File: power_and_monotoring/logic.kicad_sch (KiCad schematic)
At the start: 55 parts, among them Q1 DMN6075SQ-7, U2 LM7902D, U3 LM7902D, U4 LM7902D, U6 CD4081BM96, U7 CD4071BM96

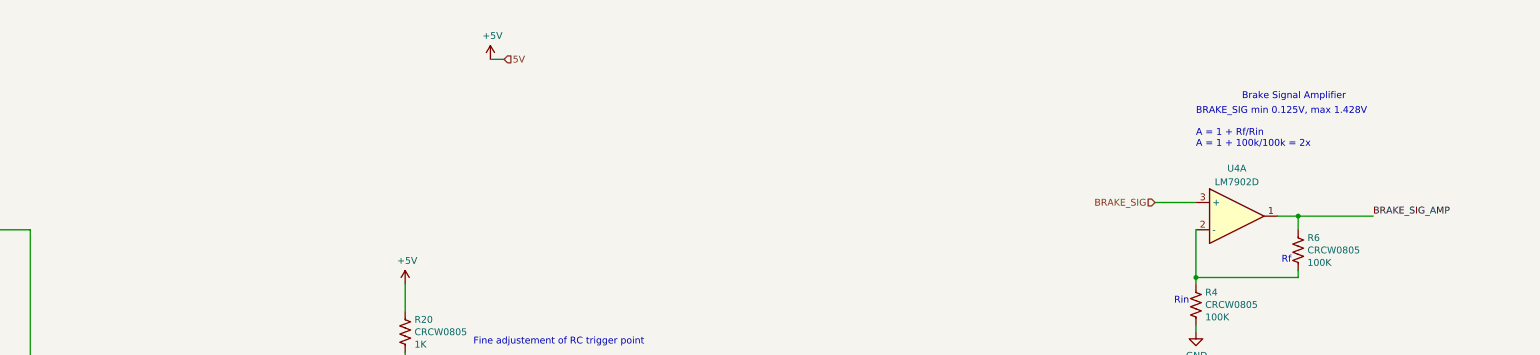
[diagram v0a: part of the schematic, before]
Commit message: first connections done (not perfect yet)
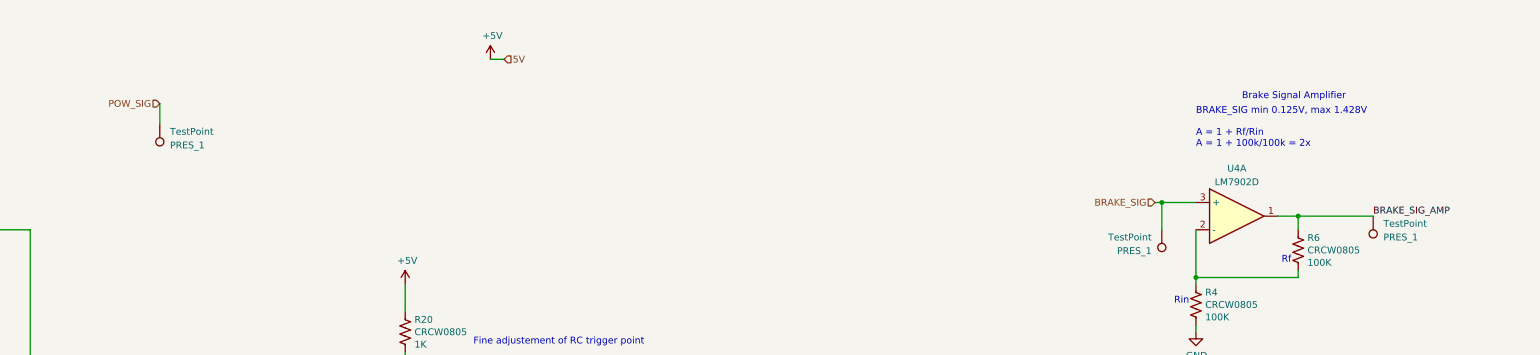
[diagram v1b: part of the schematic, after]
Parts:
- added PRES_1 (x3): TestPoint, TestPoint:TestPoint_Pad_D2.0mm, symbol Connector:TestPoint
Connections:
- net BRAKE_SIG: now also PRES_1.1
- net BRAKE_SIG_AMP: now also PRES_1.1
- net POW_SIG: now also PRES_1.1
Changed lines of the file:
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@@
   (junction (at 55.245 90.17) (diameter 0) (color 0 0 0 0)
   )
+  (junction (at 373.38 67.31) (diameter 0) (color 0 0 0 0)
+  )
   (junction (at 238.76 227.965) (diameter 0) (color 0 0 0 0)
   )
@@
     (stroke (width 0) (type default))
   )
+  (wire (pts (xy 373.38 67.31) (xy 373.38 72.39))
+    (stroke (width 0) (type default))
+  )
   (wire (pts (xy 105.41 248.92) (xy 105.41 247.65))
     (stroke (width 0) (type default))
@@
     (stroke (width 0) (type default))
   )
+  (wire (pts (xy 373.38 67.31) (xy 372.11 67.31))
+    (stroke (width 0) (type default))
+  )
   (wire (pts (xy 398.78 69.85) (xy 412.75 69.85))
     (stroke (width 0) (type default))
@@
     (stroke (width 0) (type default))
   )
+  (wire (pts (xy 186.69 48.895) (xy 186.69 52.705))
+    (stroke (width 0) (type default))
+  )
   (wire (pts (xy 105.41 161.29) (xy 105.41 161.417))
     (stroke (width 0) (type default))
@@
     (stroke (width 0) (type default))
   )
-  (wire (pts (xy 379.73 67.31) (xy 372.11 67.31))
+  (wire (pts (xy 379.73 67.31) (xy 373.38 67.31))
     (stroke (width 0) (type default))
   )
@@
     (effects (font (size 1.27 1.27)) (justify left))
   )
+  (hierarchical_label "POW_SIG" (shape input) (at 186.69 48.895 180) (fields_autoplaced)
+    (effects (font (size 1.27 1.27)) (justify right))
+  )
   (hierarchical_label "POW_SIG" (shape input) (at 67.31 53.34 180) (fields_autoplaced)
     (effects (font (size 1.27 1.27)) (justify right))
@@
     )
   )
+  (symbol (lib_id "Connector:TestPoint") (at 186.69 52.705 180) (unit 1)
+    (in_bom yes) (on_board yes) (dnp no)
+    (property "Reference" "PRES_1" (at 188.595 56.642 0)
+      (effects (font (size 1.27 1.27)) (justify right))
+    )
+    (property "Value" "TestPoint" (at 188.595 54.102 0)
+      (effects (font (size 1.27 1.27)) (justify right))
+    )
+    (property "Footprint" "TestPoint:TestPoint_Pad_D2.0mm" (at 181.61 52.705 0)
+      (effects (font (size 1.27 1.27)) hide)
+    )
+    (property "Datasheet" "~" (at 181.61 52.705 0)
+      (effects (font (size 1.27 1.27)) hide)
+    )
+    (pin "1")
+    (instances
+      (project "power_and_monotoring"
+        (path "/09bdaed7-9abd-4a06-aca9-25dcfc39eec3/52a30286-526e-4683-a1ba-aa6f0bb5d9ff"
+          (reference "PRES_1") (unit 1)
+        )
+        (path "/09bdaed7-9abd-4a06-aca9-25dcfc39eec3/22f29577-e4ea-44ad-b176-4b72d277bfff"
+          (reference "POW_SIG1") (unit 1)
+        )
+      )
+      (project "FeatherBoard"
+        (path "/e63e39d7-6ac0-4ffd-8aa3-1841a4541b55/ce4178aa-a44b-4063-8e1c-03c90baefe49"
+          (reference "TP1") (unit 1)
+        )
+      )
+    )
+  )
   (symbol (lib_id "power:GND") (at 259.08 277.495 0) (unit 1)
     (in_bom yes) (on_board yes) (dnp no)
@@
     )
   )
+  (symbol (lib_id "Connector:TestPoint") (at 373.38 72.39 0) (mirror x) (unit 1)
+    (in_bom yes) (on_board yes) (dnp no)
+    (property "Reference" "PRES_1" (at 371.475 76.327 0)
+      (effects (font (size 1.27 1.27)) (justify right))
+    )
+    (property "Value" "TestPoint" (at 371.475 73.787 0)
+      (effects (font (size 1.27 1.27)) (justify right))
+    )
+    (property "Footprint" "TestPoint:TestPoint_Pad_D2.0mm" (at 378.46 72.39 0)
+      (effects (font (size 1.27 1.27)) hide)
+    )
+    (property "Datasheet" "~" (at 378.46 72.39 0)
+      (effects (font (size 1.27 1.27)) hide)
+    )
+    (pin "1")
+    (instances
+      (project "power_and_monotoring"
+        (path "/09bdaed7-9abd-4a06-aca9-25dcfc39eec3/52a30286-526e-4683-a1ba-aa6f0bb5d9ff"
+          (reference "PRES_1") (unit 1)
+        )
+        (path "/09bdaed7-9abd-4a06-aca9-25dcfc39eec3/22f29577-e4ea-44ad-b176-4b72d277bfff"
+          (reference "BRAKE_SIG1") (unit 1)
+        )
+      )
+      (project "FeatherBoard"
+        (path "/e63e39d7-6ac0-4ffd-8aa3-1841a4541b55/ce4178aa-a44b-4063-8e1c-03c90baefe49"
+          (reference "TP1") (unit 1)
+        )
+      )
+    )
+  )
   (symbol (lib_name "+5V_1") (lib_id "power:+5V") (at 248.285 40.64 0) (unit 1)
     (in_bom yes) (on_board yes) (dnp no)
@@
         )
       )
+    )
+  )
+  (symbol (lib_id "Connector:TestPoint") (at 412.75 69.85 180) (unit 1)
+    (in_bom yes) (on_board yes) (dnp no)
+    (property "Reference" "PRES_1" (at 414.655 73.787 0)
+      (effects (font (size 1.27 1.27)) (justify right))
+    )
+    (property "Value" "TestPoint" (at 414.655 71.247 0)
+      (effects (font (size 1.27 1.27)) (justify right))
+    )
+    (property "Footprint" "TestPoint:TestPoint_Pad_D2.0mm" (at 407.67 69.85 0)
+      (effects (font (size 1.27 1.27)) hide)
+    )
+    (property "Datasheet" "~" (at 407.67 69.85 0)
+      (effects (font (size 1.27 1.27)) hide)
+    )
+    (pin "1")
+    (instances
+      (project "power_and_monotoring"
+        (path "/09bdaed7-9abd-4a06-aca9-25dcfc39eec3/52a30286-526e-4683-a1ba-aa6f0bb5d9ff"
+          (reference "PRES_1") (unit 1)
+        )
+        (path "/09bdaed7-9abd-4a06-aca9-25dcfc39eec3/22f29577-e4ea-44ad-b176-4b72d277bfff"
+          (reference "BRAKE_SIG_AMP1") (unit 1)
+        )
+      )
+      (project "FeatherBoard"
+        (path "/e63e39d7-6ac0-4ffd-8aa3-1841a4541b55/ce4178aa-a44b-4063-8e1c-03c90baefe49"
+          (reference "TP1") (unit 1)
+        )
+      )

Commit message: before design review
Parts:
- removed LED1, LED2, LED3, LED4, LED5, LED6, LED7: RED, LTST-S270KRKT, UniSA_Motorsport_Diode:0605, symbol UniSA_Motorsport_Diode:LTST-S270KRKT
- removed LED8: GREEN, LTST-S270KGKT, UniSA_Motorsport_Diode:0605, symbol UniSA_Motorsport_Diode:LTST-S270KGKT
- removed RV15 (x8): 10K, UniSA_Motorsport_Others:3296X_POT, symbol UniSA_Motorsport_Resistor:3296X-1-103LF
- added D1, D2, D3, D4, D5, D6, D7: RED, UniSA_Motorsport_Diode:0805, symbol UniSA_Motorsport_Diode:LED_0805
- added D8: GREEN, UniSA_Motorsport_Diode:0805, symbol UniSA_Motorsport_Diode:LED_0805
- added J6: 43045-1015, UniSA_Motorsport_Connector:MOLEX_43045-10YY_10PIN, symbol UniSA_Motorsport_Connector:43045-1015
- added RL1, RL2, RL3, RL4, RL5, RL6, RL7, RL8: 10 K, UniSA_Motorsport_Resistor:3296W-1, symbol UniSA_Motorsport_Resistor:3296W-1-103LF
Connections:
- net +5V: now also RL3.1, RL5.1
- net BRAKE_LIGHT_SIG: now also D8.2 (A), J6.8 (Pin_8)
- net BRAKE_SIG_AMP_HIGH: now also D2.2 (A), J6.2 (Pin_2)
- net BRAKE_SIG_AMP_SHORT_GND: now also D6.2 (A), J6.6 (Pin_6)
- net BRAKE_SIG_AMP_SHORT_HIGH: now also D5.2 (A), J6.5 (Pin_5)
- net D_BSPD_TRIGGER: now also D7.2 (A), J6.7 (Pin_7)
- net GND: now also D1.1 (K), D2.1 (K), D3.1 (K), D4.1 (K), D5.1 (K), D6.1 (K), D7.1 (K), D8.1 (K), J6.10 (Pin_10), J6.9 (Pin_9), RL1.3, RL2.3, RL4.3, RL6.3, RL7.3, RL8.3
- net POWER_SIG_HIGH: now also D1.2 (A), J6.1 (Pin_1)
- net POWER_SIG_SHORT_GND: now also D4.2 (A), J6.4 (Pin_4)
- net POWER_SIG_SHORT_HIGH: now also D3.2 (A), J6.3 (Pin_3)
- net at R20.2: now also RL7.1
- net at PRES_1.1, U3.12 (+): now also RL7.2
- net at R3.2: now also RL8.1
- net at PRES_1.1, U2.6 (-): now also RL1.2
- net at PRES_1.1, U2.13 (-): now also RL3.2
- net at R9.1: now also RL3.3
- net at PRES_1.1, U3.6 (-): now also RL5.2
- net at PRES_1.1, U3.3 (+): now also RL4.2
- net at R11.1: now also RL5.3
- net at R10.2: now also RL4.1
- net at R8.2: now also RL2.1
- net at PRES_1.1, U2.2 (-): now also RL8.2
- net at R12.2: now also RL6.1
- net at PRES_1.1, U3.10 (+): now also RL6.2
- net at PRES_1.1, U2.9 (-): now also RL2.2
- net at R7.2: now also RL1.1

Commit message: Final
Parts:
- removed C3: GCM0805_1u, UniSA_Motorsport_Capacitor:0805, symbol UniSA_Motorsport_Capacitor:GCM0805_1u
- removed PRES_1: TestPoint, TestPoint:TestPoint_Pad_D2.0mm, symbol Connector:TestPoint
- removed R10, R11, R12, R20, R8, R9: CRCW0805, UniSA_Motorsport_Resistor:0805, symbol UniSA_Motorsport_Resistor:CRCW0805
- removed U6: CD4081BM96, UniSA_Motorsport_SO:SOIC-14, symbol UniSA_Motorsport_Logic:CD4081BM96
- added BRAKE_SIG_AMP1: TestPoint, TestPoint:TestPoint_Pad_D2.0mm, symbol Connector:TestPoint
- added R29, R30, R50, R51: CRCW0805, UniSA_Motorsport_Resistor:0805, symbol UniSA_Motorsport_Resistor:CRCW0805
- added U1: 74LVC1G08GW,125, UniSA_Motorsport_SO:TSSOP-5, symbol UniSA_Motorsport_Logic:74LVC1G08GW,125
- R13, R14, R15, R16, R17, R18: Resistance 150R -> 470R
- R21, R5: Resistance 100R -> 470R
- R3: Resistance 1K -> 2.2K
- R4, R6: Resistance 100K -> 10K
- renumbered PRES_1 to BRAKE_SIG1, PRES_1 to BREAK_HIGH1, PRES_1 to BREAK_LOW1, PRES_1 to BREAK_PRESSED1, PRES_1 to BREAK_SIG1, C4 to C2, C4 to C3, C4 to C5, D7 to D1, D1 to D2, D2 to D3, D3 to D4, D4 to D5, D5 to D6, D6 to D7, PRES_1 to POW_HIGH1, PRES_1 to POW_LOW1, PRES_1 to POW_PRESSED1, PRES_1 to POW_SIG_AMP1, PRES_1 to RC_TRIG1
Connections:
- net +5V: now also U1.5 (VCC); no longer C5.1, R3.1, R7.1, RL3.1, RL5.1, U4.4 (VDD)
- net BRAKE_LIGHT_SIG: now also Q1.1 (G), R5.1, U2.1; no longer D8.2 (A), R5.2
- net BRAKE_SIG_AMP: now also U4.13 (-), U4.14, BRAKE_SIG_AMP1.1; no longer R6.1, U4.1
- net BRAKE_SIG_AMP_HIGH: now also R14.1, U2.8, U1.2; no longer D3.2 (A), R14.2
- net BRAKE_SIG_AMP_SHORT_GND: now also R18.1, U3.8, U7.6; no longer D7.2 (A), R18.2
- net BRAKE_SIG_AMP_SHORT_HIGH: now also R17.1, U3.7, U7.5; no longer D6.2 (A), R17.2
- net BSPD_TRIGGER: now also J6.7 (Pin_7)
- net GND: now also R3.2, RL3.3, RL5.3, R30.2, R51.2, U1.3 (GND); no longer U4.10 (+), U4.12 (+), U4.5 (+)
- net POWER_SIG_HIGH: now also R13.1, U2.7, U1.1; no longer D2.2 (A), R13.2
- net POWER_SIG_SHORT_GND: now also R16.1, U3.1, U7.2; no longer D5.2 (A), R16.2
- net POWER_SIG_SHORT_HIGH: now also R15.1, U2.14, U7.1; no longer D4.2 (A), R15.2
- net POW_SIG: now also U4.5 (+); no longer POW_SIG_AMP1.1, U2.12 (+), U2.5 (+), U3.2 (-)
- net +3.3V: now reaches RL8.1
- net +3.3V: now also RL1.1, RL2.1, RL3.1, RL4.1, RL5.1, RL6.1, RL7.1; no longer R3.2
- net at U7.12: now also U1.4
- net at R7.2: now also R19.1, R3.1; no longer RL1.1
- net POW_SIG_AMP: now reaches U4.8, U4.9 (-)
- net POW_SIG_AMP: now also POW_SIG_AMP1.1, U2.12 (+), U2.5 (+), U3.2 (-)
- net at U7.11: now also R7.1; no longer R19.1
- net at U4.6 (-), U4.7: now also R29.1
- net D_BSPD_TRIGGER: no longer names the net of D1.2 (A), R21.2
- net D_BSPD_TRIGGER: no longer J6.7 (Pin_7)
- new net: D4.2 (A), R15.2
- new net: D7.2 (A), R18.2
- new net: D8.2 (A), R5.2
- new net: R29.2, R30.1, U4.10 (+)
- new net: D2.2 (A), R13.2
- new net: R50.1, R6.1, U4.1
- new net: R50.2, R51.1, U4.12 (+)
- new net: D5.2 (A), R16.2
- new net: D6.2 (A), R17.2
- new net: D3.2 (A), R14.2
- new net 12V: C5.1, U4.4 (VDD)
- no-connect marks 3 -> 0
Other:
- note added: "Leave unconected"
- note added: "R1"
- note added: "R2"
- note added: "Vout=Vin*(R2)/(R1+R2)"
- note removed: "Unused Logic"
- moved on the sheet: BRAKE_SIG1, J6, POW_SIG_AMP1, R4, R6, U4A, U4B, U4C, U4D

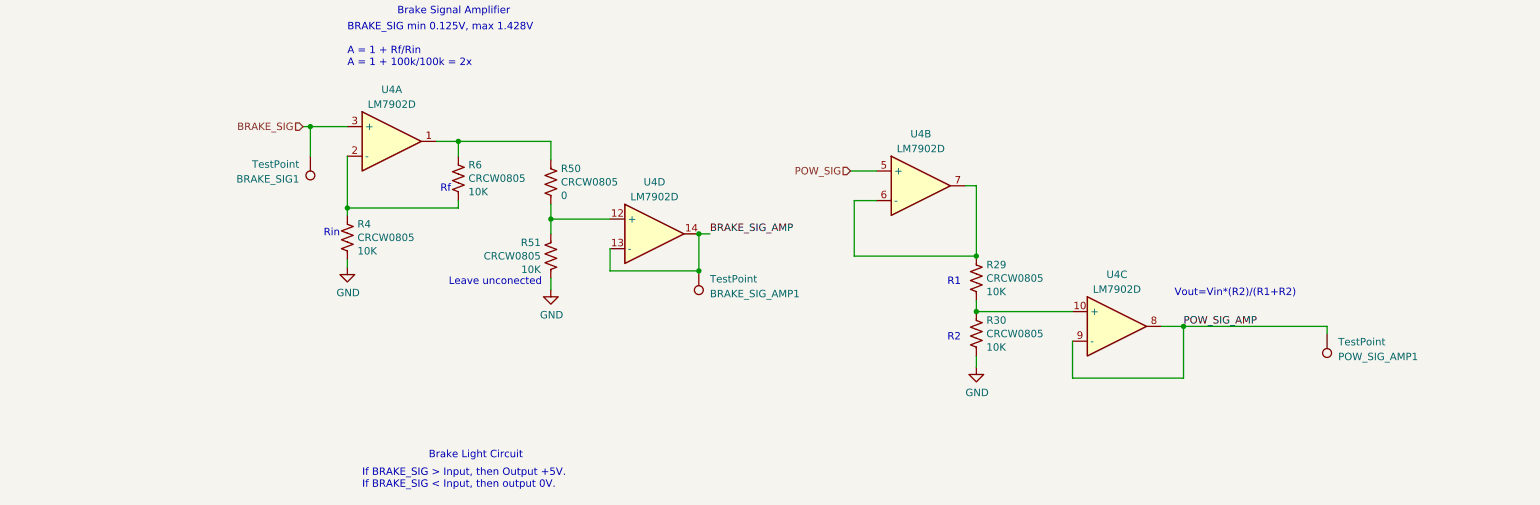
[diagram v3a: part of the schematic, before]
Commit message: Made it 4 layers
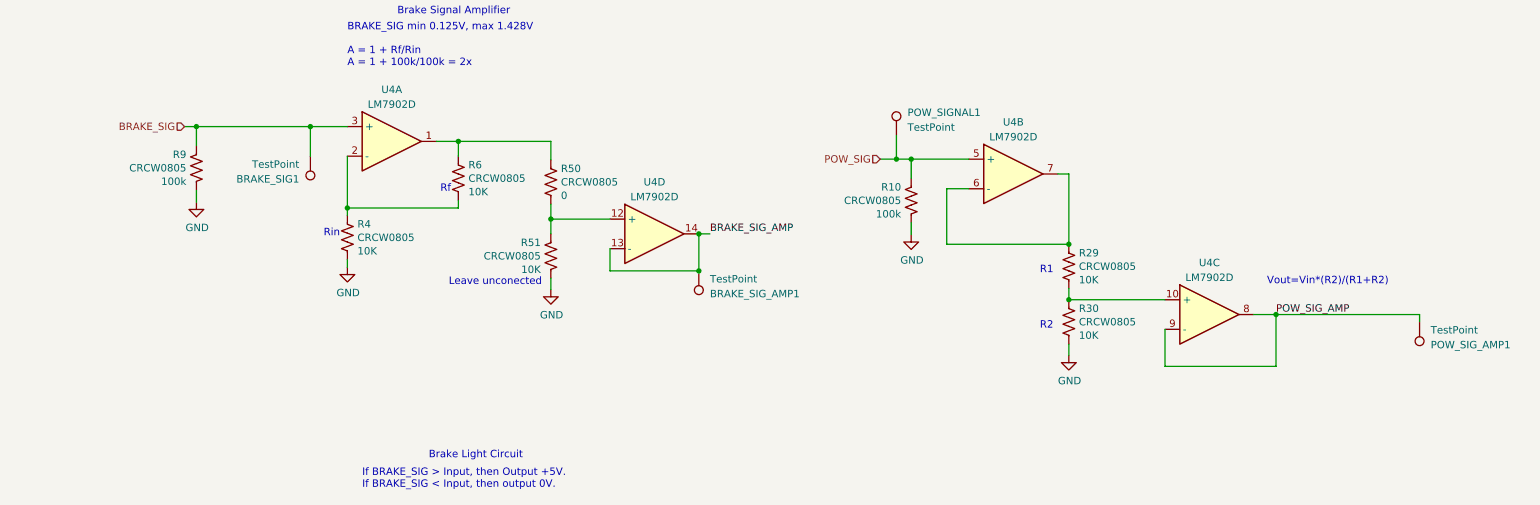
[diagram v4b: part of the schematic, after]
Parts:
- added POW_SIGNAL1: TestPoint, TestPoint:TestPoint_Pad_D2.0mm, symbol Connector:TestPoint
- added R10, R9: CRCW0805, UniSA_Motorsport_Resistor:0805, symbol UniSA_Motorsport_Resistor:CRCW0805
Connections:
- net BRAKE_SIG: now also R9.1
- net GND: now also R10.2, R9.2
- net POW_SIG: now also POW_SIGNAL1.1, R10.1
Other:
- moved on the sheet: POW_SIG_AMP1, R29, R30, U4B, U4C
